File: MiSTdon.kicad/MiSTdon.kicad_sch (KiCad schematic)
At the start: 32 parts, among them J1 Conn_02x06_Top_Bottom, J10 Conn_01x03, J11 Conn_01x05, J2 Conn_01x12, J3 Conn_01x05, J4 Conn_02x10_Odd_Even, J5 Conn_02x10_Odd_Even, J6 Conn_01x06, J7 Conn_02x06_Top_Bottom, J8 DB9_Male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

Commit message: pcb draft
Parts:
- removed J6: Conn_01x06, symbol Connector_Generic:Conn_01x06
- added J6: Conn_02x03_Odd_Even, Connector_PinHeader_2.54mm:PinHeader_2x03_P2.54mm_Vertical, symbol Connector_Generic:Conn_02x03_Odd_Even
- D1: footprint (none) -> Diode_SMD:D_0805_2012Metric_Pad1.15x1.40mm_HandSolder
- J1: footprint (none) -> libraries:Pmod_2x06_P2.54mm_Vertical_2
- J10: footprint (none) -> Connector_PinHeader_2.54mm:PinHeader_1x03_P2.54mm_Vertical
- J11: footprint (none) -> Connector_PinHeader_2.54mm:PinHeader_1x05_P2.54mm_Vertical
- J2: footprint (none) -> Connector_PinSocket_2.54mm:PinSocket_1x12_P2.54mm_Vertical
- J3: footprint (none) -> Connector_PinSocket_2.54mm:PinSocket_1x05_P2.54mm_Vertical
- J4, J5: footprint (none) -> Connector_PinSocket_2.54mm:PinSocket_2x10_P2.54mm_Vertical
- J7: footprint (none) -> libraries:PMOD_Female_Horizontal_2
- J8, J9: footprint (none) -> Connector_Dsub:DSUB-9_Male_Horizontal_P2.77x2.84mm_EdgePinOffset9.90mm_Housed_MountingHolesOffset11.32mm
- JP1, JP3, JP4, JP5: footprint (none) -> Connector_PinHeader_2.54mm:PinHeader_1x02_P2.54mm_Vertical
- JP2: footprint (none) -> Jumper:SolderJumper-3_P1.3mm_Open_RoundedPad1.0x1.5mm
- R1, R10, R11, R12, R2, R3, R4, R5, R6, R7, R8, R9: footprint (none) -> Resistor_SMD:R_0805_2012Metric_Pad1.20x1.40mm_HandSolder
- SW1, SW3, SW4: footprint (none) -> Button_Switch_THT:SW_PUSH_6mm_H5mm
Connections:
- net 3V3: now also J6.5 (Pin_5)
- net 5V: now also J6.1 (Pin_1), J6.2 (Pin_2)
- net GND: now also J6.3 (Pin_3), J6.4 (Pin_4)
- net NRST: now also J6.6 (Pin_6)
- net NRST2: now also J7.1 (Pin_1); no longer J7.7 (Pin_7)
- net PA10_SS2: now also J7.4 (Pin_4); no longer J7.10 (Pin_10)
- net PA12_MISO: now also J7.9 (Pin_9); no longer J7.3 (Pin_3)
- net PA13_MOSI: now also J7.8 (Pin_8); no longer J7.2 (Pin_2)
- net PA14_SCK: now also R1.2; no longer R1.1
- net PA2_SS4: now also J7.2 (Pin_2); no longer J7.8 (Pin_8)
- net PA3_SS3: now also J7.7 (Pin_7); no longer J7.1 (Pin_1)
- net PA9_CONF_D0: now also J7.3 (Pin_3); no longer J7.9 (Pin_9)
- net SCK1: now reaches J2.4 (Pin_4), R3.1
- net VBUS: now reaches J3.1 (Pin_1), JP1.2 (Pin_2)
- net CD: now reaches J1.9 (Pin_9), JP2.3 (B)
- net SCK2: now reaches J1.4 (Pin_4), R2.2
- net TCK renamed PB7_TCK
- net TDI renamed PB4_TDI
- net TDO renamed PB5_TDO
- net TMS renamed PB6_TMS
- new net SCK3: J7.10 (Pin_10), R1.1
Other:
- note removed: "VBUS"
- moved on the sheet: D1, R1, R12

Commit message: Kicad done, missing routing
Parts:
- removed J11: Conn_01x05, Connector_PinHeader_2.54mm:PinHeader_1x05_P2.54mm_Vertical, symbol Connector_Generic:Conn_01x05
- removed JP3: Conn_01x02, Connector_PinHeader_2.54mm:PinHeader_1x02_P2.54mm_Vertical, symbol Connector_Generic:Conn_01x02
- added J11: Conn_01x06, Connector_PinHeader_2.54mm:PinHeader_1x06_P2.54mm_Vertical, symbol Connector_Generic:Conn_01x06
- added JP3: Conn_01x03, Connector_PinHeader_2.54mm:PinHeader_1x03_P2.54mm_Vertical, symbol Connector_Generic:Conn_01x03
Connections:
- net GND: now also J11.6 (Pin_6), JP3.3 (Pin_3)
- net NRST: now also JP3.1 (Pin_1)
- net NRST2: now also JP3.2 (Pin_2)
- net PA15_CONF_DCLK: now also J11.1 (Pin_1)
- net PA4_CONF_DONE: now also J11.4 (Pin_4)
- net PA7_CONF_NSTAT: now also J11.3 (Pin_3)
- net PA8_CONF_NCFG: now also J11.2 (Pin_2)
- net PA9_CONF_D0: now also J11.5 (Pin_5)
- net PB2_AD6 renamed PB2_AD6_OSD
- net PB3_AD7 renamed PB3_AD7_USER
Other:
- note added: "(**)"
- note added: "Joystick 0"
- note added: "Joystick 1"
- note added: "POWER SUPPLY FROM SAM7S (**) (OPTIONAL)"
- note removed: "(OPTIONAL) POWER SUPPLY FROM SAM7S (**)"
- moved on the sheet: J10, J6, J7, R1, R10, R11, R9

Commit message: v0.7 PCB gerbers generated for manufacturing
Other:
- title: (none) -> MiSTdon
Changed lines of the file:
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@@
 (kicad_sch (version 20211123) (generator eeschema)
   (paper "A4")
+  (title_block
+    (title "MiSTdon")
+    (date "2023-02-25")
+    (rev "${VERSION}")
+    (comment 2 "2023 @somhi <@somhic at telegram>")
+    (comment 3 "License: CC-BY-SA v4.0")
+  )
   (junction (at 128.905 137.795) (diameter 0) (color 0 0 0 0)
   )

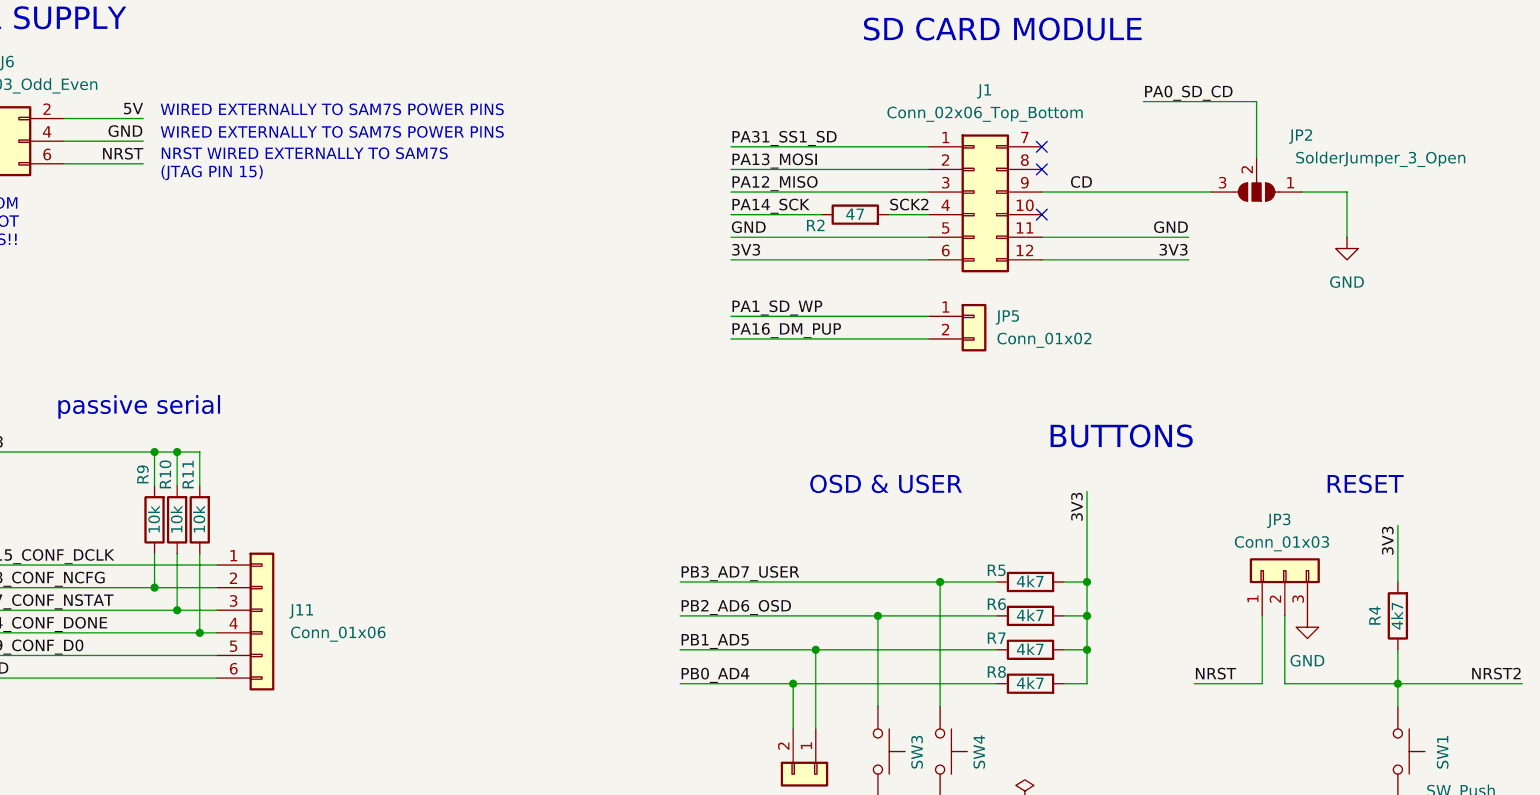
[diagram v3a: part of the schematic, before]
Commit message: v0.8 some changes after testing first PCB
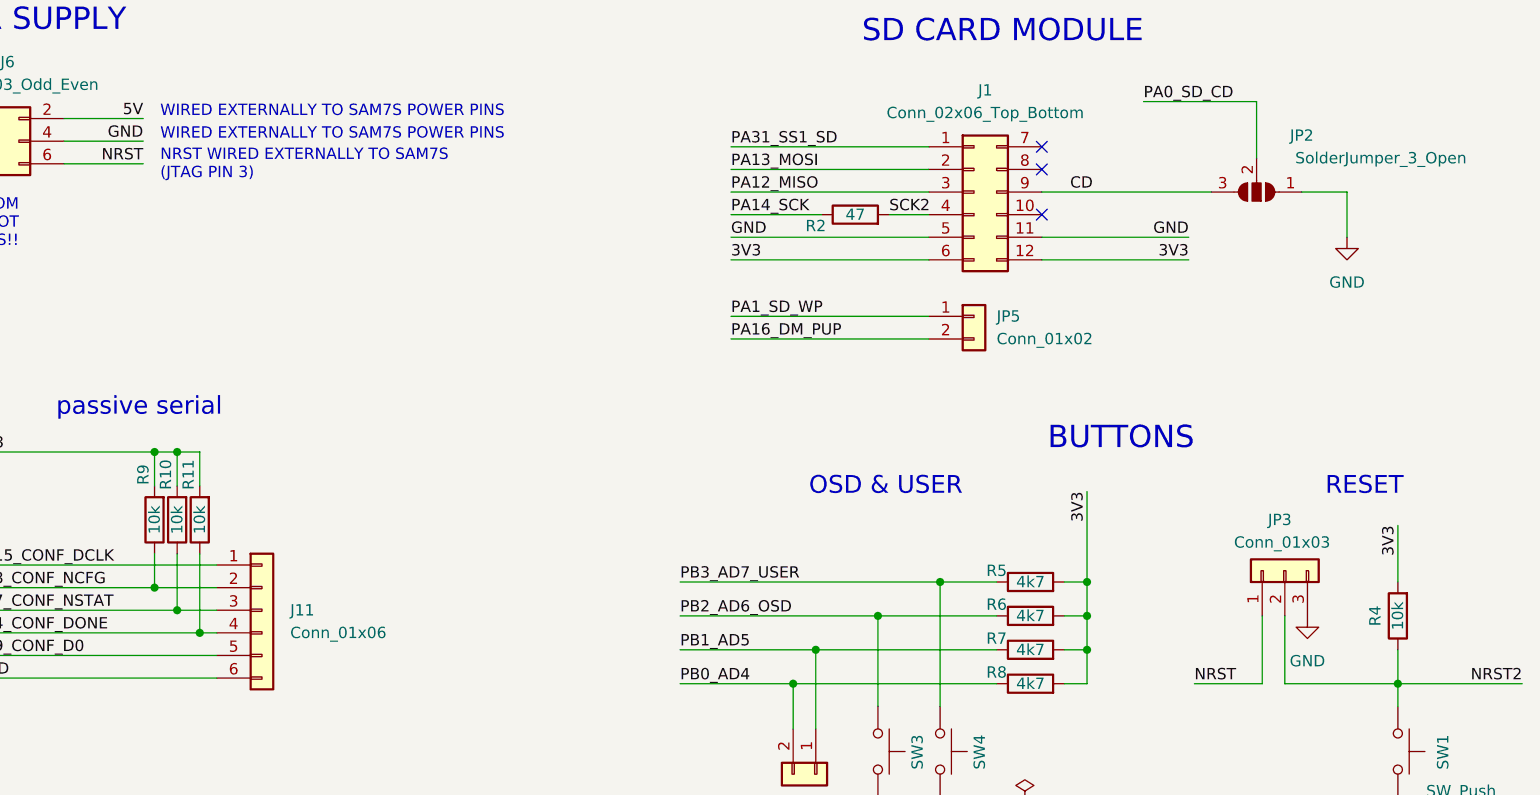
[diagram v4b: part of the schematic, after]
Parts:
- R4: value 4k7 -> 10k
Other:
- note added: "NRST WIRED EXTERNALLY TO SAM7S (JTAG PIN 3)"
- note removed: "NRST WIRED EXTERNALLY TO SAM7S (JTAG PIN 15)"
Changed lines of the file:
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@@
     (effects (font (size 1.27 1.27)) (justify left bottom))
   )
-  (text "NRST WIRED EXTERNALLY TO SAM7S\n(JTAG PIN 15)" (at 124.46 86.995 0)
+  (text "NRST WIRED EXTERNALLY TO SAM7S\n(JTAG PIN 3)" (at 124.46 86.995 0)
     (effects (font (size 1.27 1.27)) (justify left bottom))
   )
@@
     (in_bom yes) (on_board yes)
     (property "Reference" "R4" (id 0) (at 260.985 135.89 90))
-    (property "Value" "4k7" (id 1) (at 263.525 135.89 90))
+    (property "Value" "10k" (id 1) (at 263.525 135.89 90))
     (property "Footprint" "Resistor_SMD:R_0805_2012Metric_Pad1.20x1.40mm_HandSolder" (id 2) (at 265.303 135.89 90)
       (effects (font (size 1.27 1.27)) hide)
@@
     )
     (path "/f677df2f-4fe9-4024-86d0-81bc350e2153"
-      (reference "R4") (unit 1) (value "4k7") (footprint "Resistor_SMD:R_0805_2012Metric_Pad1.20x1.40mm_HandSolder")
+      (reference "R4") (unit 1) (value "10k") (footprint "Resistor_SMD:R_0805_2012Metric_Pad1.20x1.40mm_HandSolder")
     )
     (path "/3bc46acc-a8f5-4209-b62d-5879414cc872"
